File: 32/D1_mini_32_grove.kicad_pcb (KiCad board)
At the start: 2 copper layers, 31.6 x 37 mm, 9 parts, among them J1 Conn_01x04_Pin, J2 Conn_01x04_Pin, J3 Conn_01x04_Pin, J4 Conn_01x04_Pin, U1 esp32-wemos-d1-mini

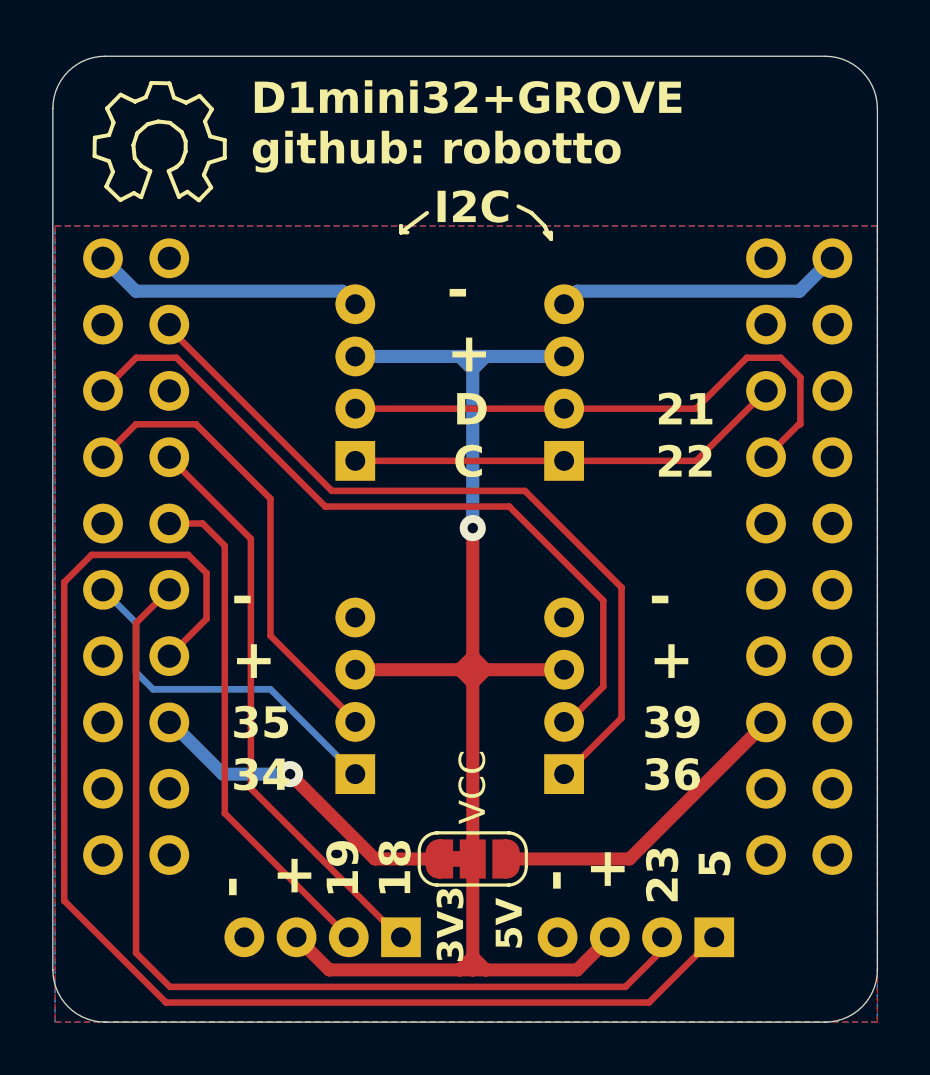
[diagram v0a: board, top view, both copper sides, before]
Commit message: Added a switch for VCC selector instead of solder bridge.. its tight but itll work
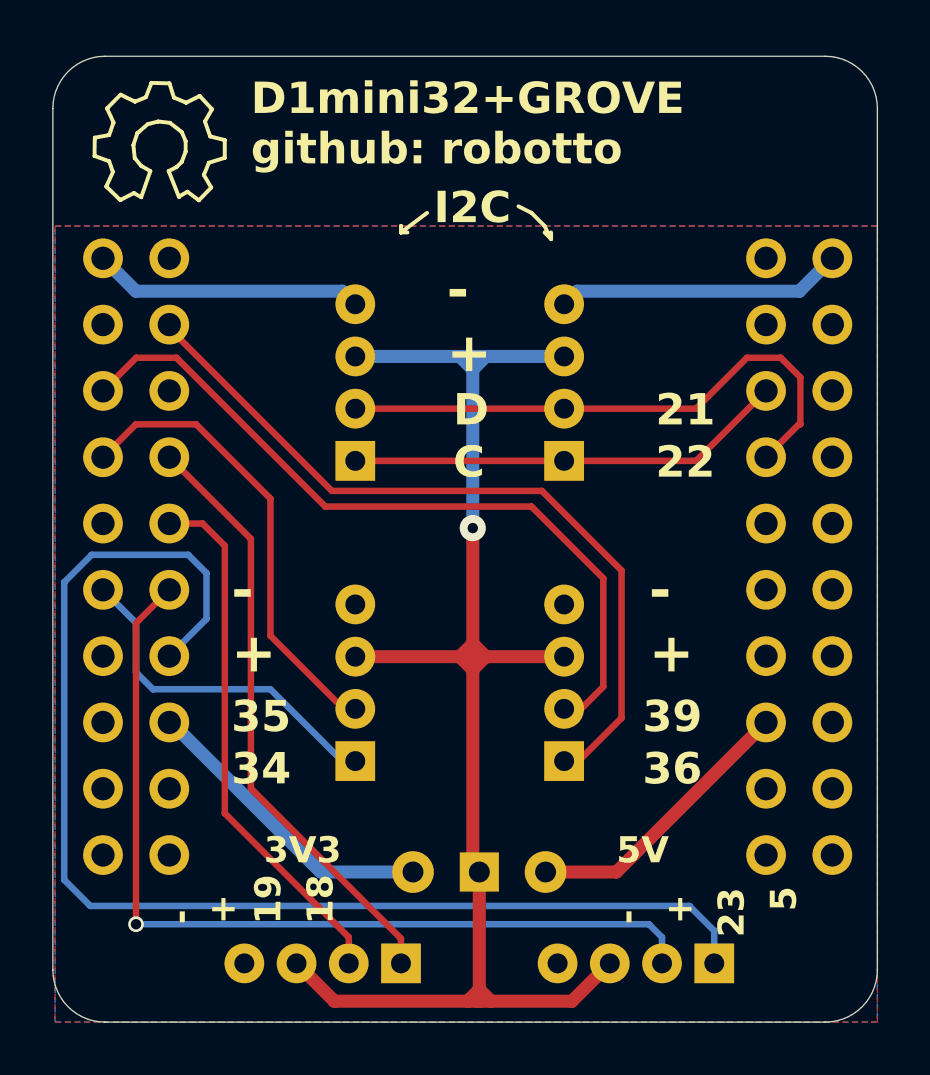
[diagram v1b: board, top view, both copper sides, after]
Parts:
- removed VCC: SolderJumper_3_Bridged12, Jumper:SolderJumper-3_P1.3mm_Bridged12_RoundedPad1.0x1.5mm_NumberLabels
- added SW1: SW_Wuerth_450301014042, Button_Switch_THT:SW_Slide-03_Wuerth-WS-SLTV_10x2.5x6.4_P2.54mm, F.Cu at (113.2, 76.2)
- moved J3 1.00 mm to (110.2, 79.8)
- moved J4 1.00 mm to (122.2, 79.8)
- moved J1 0.50 mm to (116.5, 72.0)
- moved J2 0.50 mm to (108.5, 72.0)
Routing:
- net /IO23: track 36.2 -> 34.7 mm, vias 0 -> 1
- net /IO5: track 49.7 -> 48.3 mm
- net VCC: track 58.2 -> 59.5 mm
- net +5V: track 12.1 -> 10.8 mm
- net /IO19: track 19.4 -> 20.4 mm
- net /IO18: track 22.1 -> 23.1 mm
- net +3.3V: track 12.5 -> 11.7 mm, vias 1 -> 0

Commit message: Messing with silkscreen, mostly
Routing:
- net /SDA: track 21.8 -> 16.5 mm
- net GND: track 21.4 -> 22.4 mm
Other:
- board text added: "VCC"
- board text removed: "+"
- board text removed: "-"

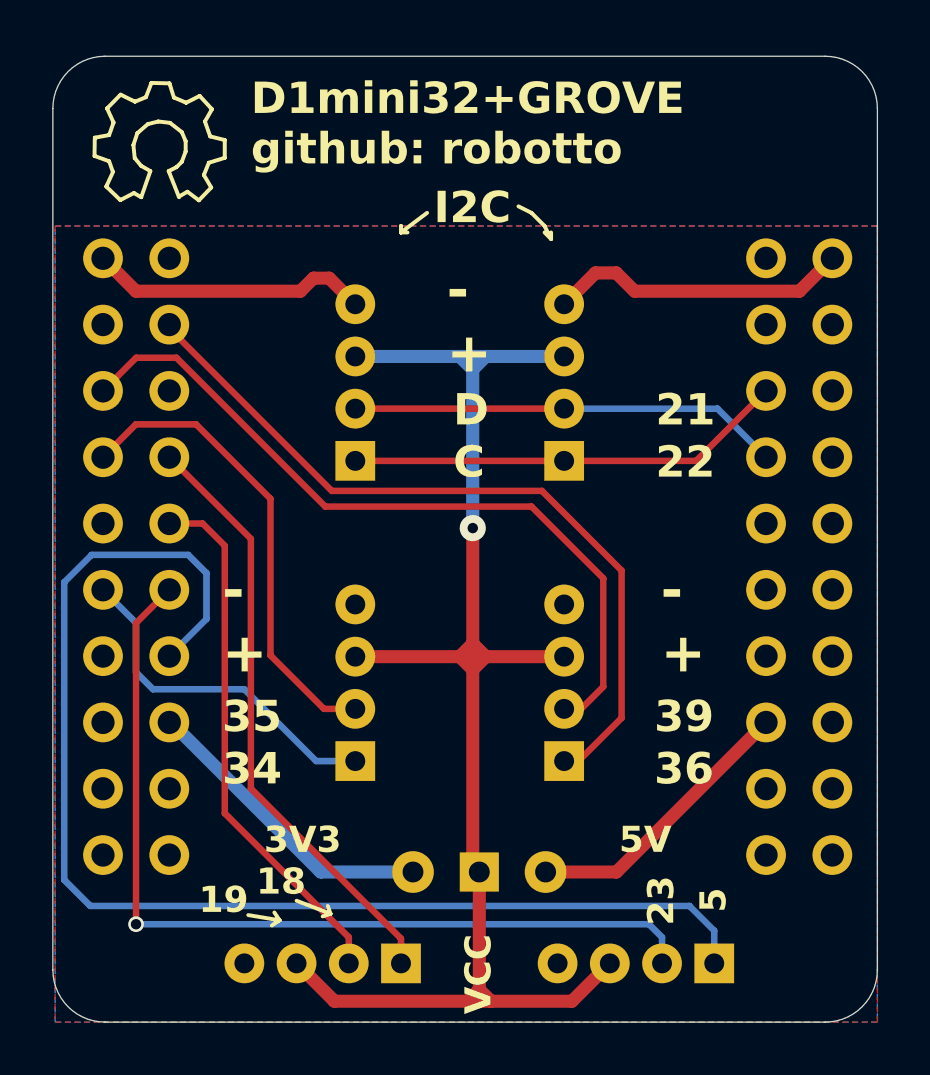
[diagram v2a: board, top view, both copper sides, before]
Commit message: The 32board had room for one more grove connector... finetuned some 3D stuff too
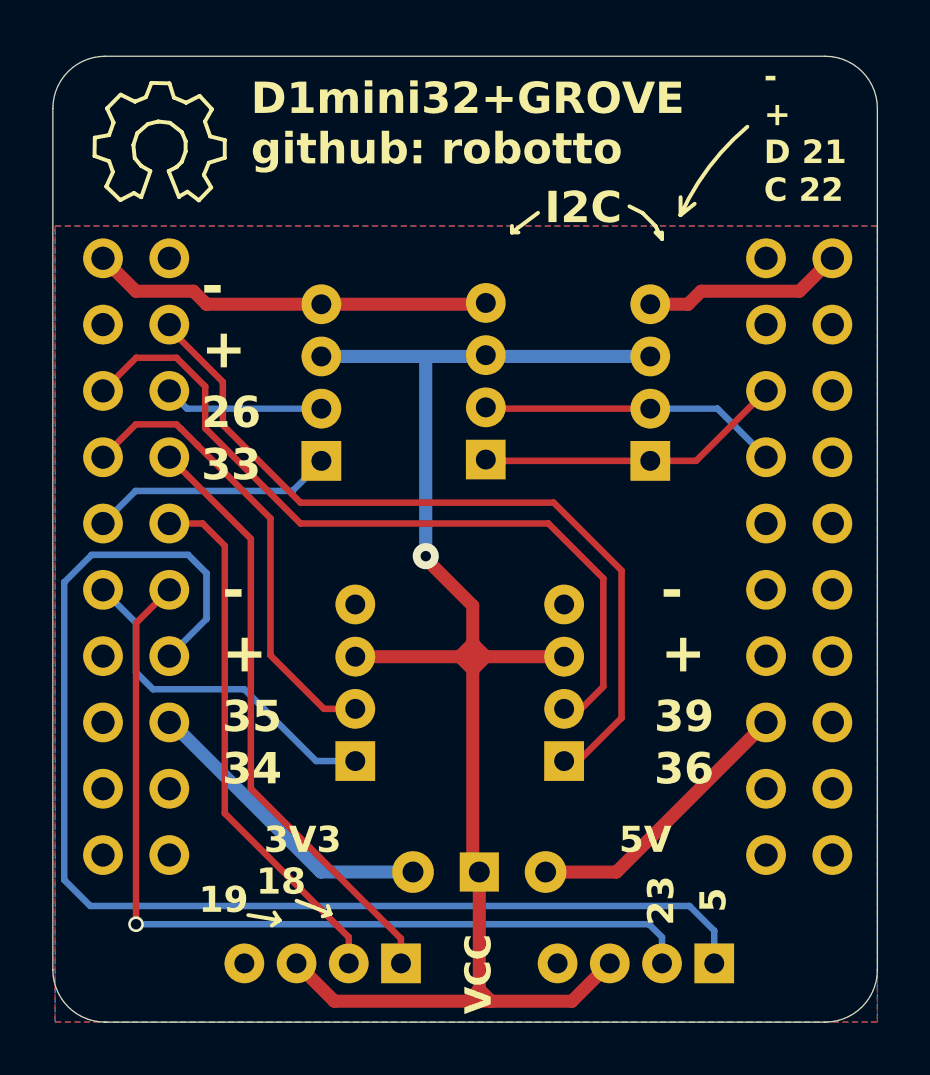
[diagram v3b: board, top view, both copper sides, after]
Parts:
- added J5: Conn_01x04_Pin, pretty:NS-Tech_Grove_1x04_P2mm_Vertical, F.Cu at (107.2, 60.5)
- moved I2C_2 5.00 mm to (113.5, 60.5)
- moved I2C_1 3.30 mm to (119.8, 60.5)
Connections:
- U1 pad 6: unconnected-(U1-IO_26/D0-Pad6) -> Net-(J5-Pin_2)
- U1 pad 9: unconnected-(U1-IO_33-Pad9) -> Net-(J5-Pin_1)
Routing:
- net Net-(J5-Pin_1): track 0.00 -> 9.39 mm
- net VCC: track 59.5 -> 65.8 mm
- net Net-(J5-Pin_2): track 0.00 -> 6.11 mm
- net /SCL: track 16.8 -> 11.9 mm
- net /SDA: track 16.5 -> 11.5 mm
- net /IO36: track 30.0 -> 31.0 mm
- net /IO39: track 29.3 -> 30.2 mm
- net GND: track 22.4 -> 23.1 mm
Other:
- board text added: "- + D 21 C 22"
- board text added: "26"
- board text added: "33"
- board text removed: "21"
- board text removed: "22"
- board text removed: "C"
- board text removed: "D"

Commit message: 3D stuff
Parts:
- U1: value esp32-wemos-d1-mini -> e
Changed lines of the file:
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@@
 		)
 		(embedded_fonts no)
-		(model "/Users/robotto/Hack/D1-mini-grove-shield/lib/Vertical slide switch SS-12D00G3 High Knob 3mm SPDT v2.step"
+		(model "${KIPRJMOD}/../lib/Vertical slide switch SS-12D00G3 High Knob 3mm SPDT v2.step"
 			(offset
 				(xyz 0 0 0)
@@
 			)
 		)
-		(property "Value" "esp32-wemos-d1-mini"
+		(property "Value" "e"
 			(at -25.75 0.75 90)
 			(layer "F.Fab")
+			(hide yes)
 			(effects
 				(font
@@
 		)
 		(embedded_fonts no)
-		(model "${KIPRJMOD}/kicad-esp32-wemos-d1-mini/esp32-wemos-d1-mini.step"
-			(hide yes)
+		(model "${KICAD9_3DMODEL_DIR}/Connector_PinHeader_2.54mm.3dshapes/PinHeader_2x10_P2.54mm_Vertical.wrl"
 			(offset
-				(xyz 137.25 42.7 -32.5)
+				(xyz -11.4 11.4 -1.6)
 			)
 			(scale
@@
 			)
 			(rotate
-				(xyz -90 0 0)
-			)
-		)
+				(xyz -0 -180 -0)
+			)
+		)
+		(model "${KICAD9_3DMODEL_DIR}/Connector_PinHeader_2.54mm.3dshapes/PinHeader_2x10_P2.54mm_Vertical.wrl"
+			(offset
+				(xyz 14 11.4 -1.6)
+			)
+			(scale
+				(xyz 1 1 1)
+			)
+			(rotate
+				(xyz -0 -180 -0)
+			)
+		)

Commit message: Second production run
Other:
- board text added: "HUSK AT SPISE!"
- board text added: "Husk at lave flowcharts!"
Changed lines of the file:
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@@
+		)
+	)
+	(gr_text "Husk at lave flowcharts!"
+		(at 117.8 56.8 70)
+		(layer "B.SilkS")
+		(effects
+			(font
+				(size 1 1)
+				(thickness 0.15)
+			)
+			(justify left bottom mirror)
+		)
+	)
+	(gr_text "HUSK AT SPISE!"
+		(at 124.5 50 0)
+		(layer "B.SilkS")
+		(effects
+			(font
+				(size 2 2)
+				(thickness 0.25)
+			)
+			(justify left bottom mirror)
 		)
 	)
